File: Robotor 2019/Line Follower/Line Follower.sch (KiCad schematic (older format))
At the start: 70 parts, among them J1 Conn_01x03_Male, J2 Conn_01x04_Female, J3 USB_B_Mini, J7 Conn_01x03_Female, J8 Conn_01x03_Female, M1 Motor_DC, M2 Motor_DC, U1 AMS1117-3V3, U2 AMS1117-3V3, U3 AMS1117-5.0, U4 STM32F103C8Tx, U5 ITR8307, U6 L298P, U7 ITR8307, U8 ITR8307, U9 ITR8307, Y1 32.768Khz, Y2 8Mhz

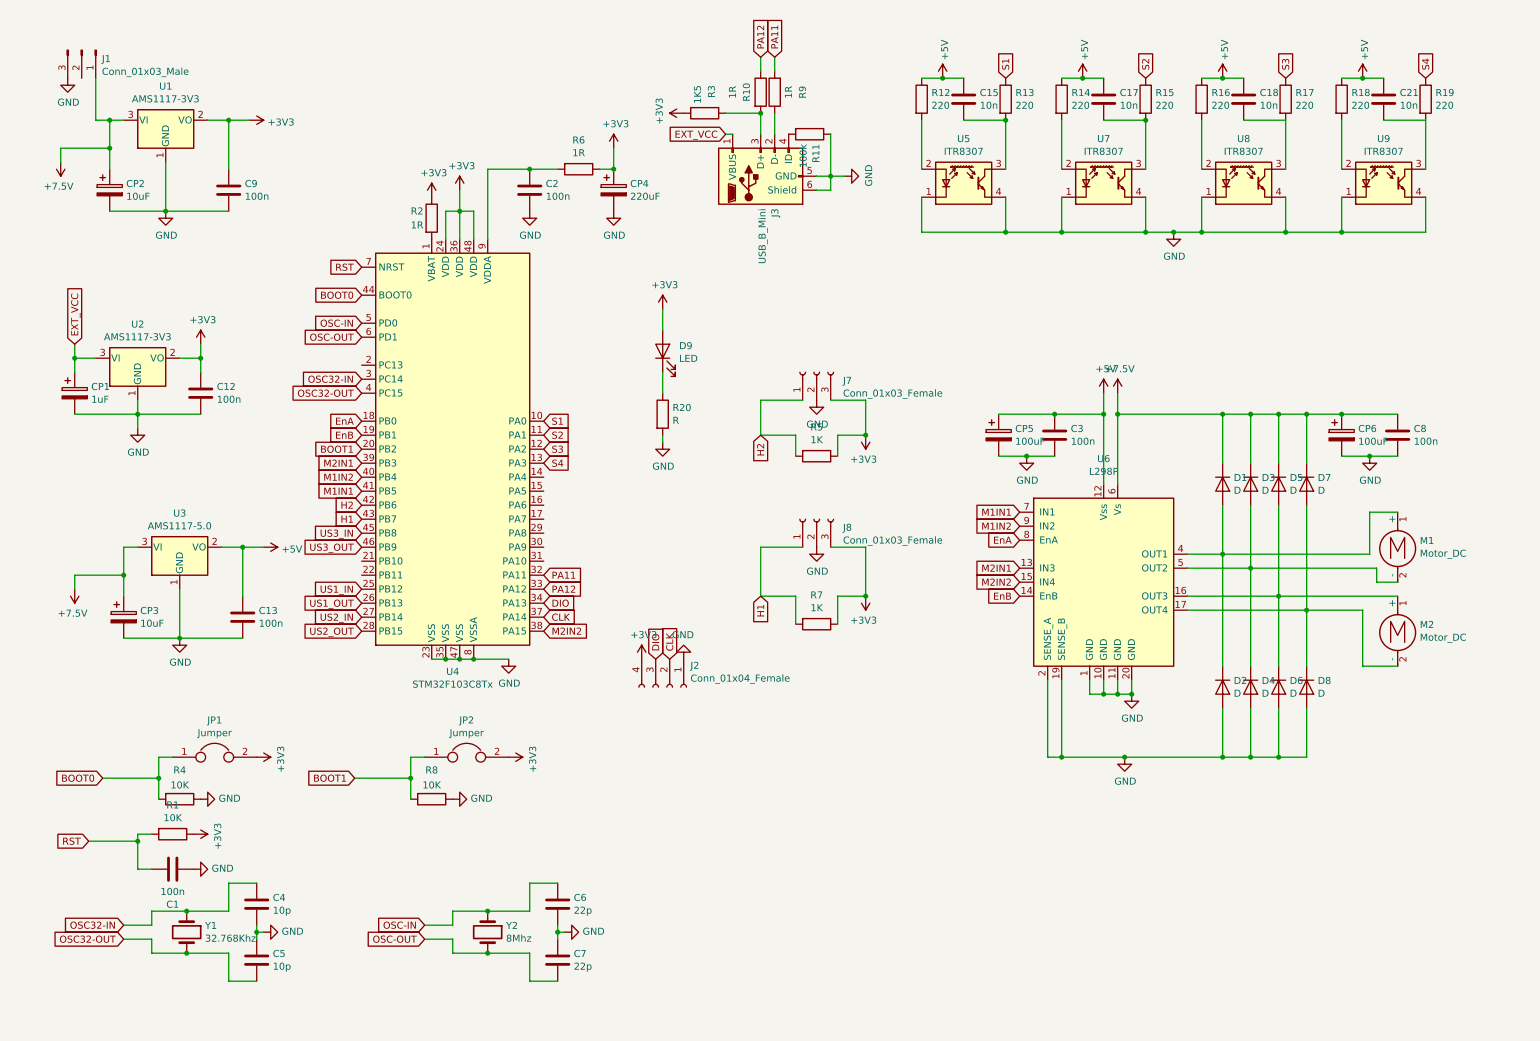
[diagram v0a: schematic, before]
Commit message: Hopefully it works, Line Follower scheme added.
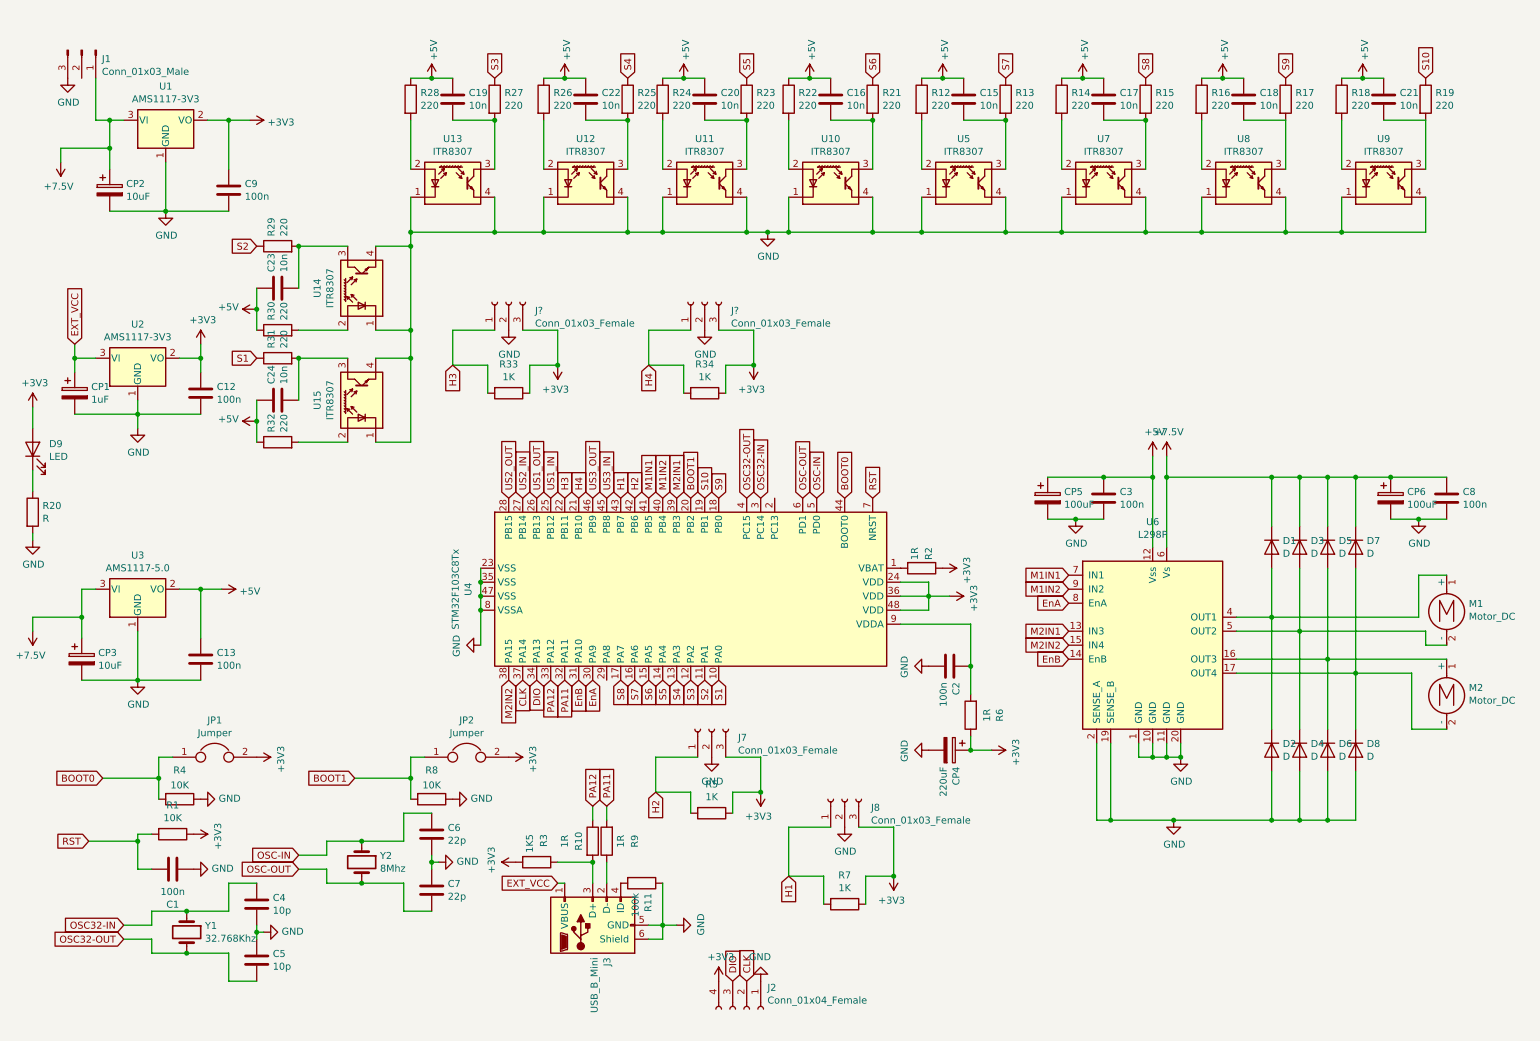
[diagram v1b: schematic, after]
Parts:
- added C16, C19, C20, C22, C23, C24: 10n, Capacitor_SMD:C_0805_2012Metric_Pad1.15x1.40mm_HandSolder, symbol Device:C
- added J? (x2): Conn_01x03_Female, Connector_PinHeader_2.54mm:PinHeader_1x03_P2.54mm_Vertical, symbol Connector:Conn_01x03_Female
- added R21, R22, R23, R24, R25, R26, R27, R28, R29, R30, R31, R32: 220, Resistor_SMD:R_0805_2012Metric_Pad1.15x1.40mm_HandSolder, symbol Device:R
- added R33, R34: 1K, Resistor_SMD:R_0805_2012Metric_Pad1.15x1.40mm_HandSolder, symbol Device:R
- added U10, U11, U12, U13, U14, U15: ITR8307, OptoDevice:Everlight_ITR8307, symbol Sensor_Proximity:ITR8307
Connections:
- net +3V3: now also J?.3 (Pin_3), J?.3 (Pin_3), R33.1, R34.1
- net +5V: now also C16.1, C19.1, C20.1, C22.1, C23.1, C24.1, R22.1, R24.1, R26.1, R28.1, R30.1, R32.1
- net EnA: now also U4.30 (PA9); no longer U4.18 (PB0)
- net EnB: now also U4.31 (PA10); no longer U4.19 (PB1)
- net GND: now also J?.2 (Pin_2), J?.2 (Pin_2), U10.1 (K), U10.4 (E), U11.1 (K), U11.4 (E), U12.1 (K), U12.4 (E), U13.1 (K), U13.4 (E), U14.1 (K), U14.4 (E), U15.1 (K), U15.4 (E)
- net S1: now also R31.1; no longer R13.1
- net S2: now also R29.1; no longer R15.1
- net S3: now also R27.1; no longer R17.1
- net S4: now also R25.1; no longer R19.1
- net S5: now reaches U4.14 (PA4)
- net S5: now also R23.1
- net S6: now reaches U4.15 (PA5)
- net S6: now also R21.1
- net S7: now reaches U4.16 (PA6)
- net S7: now also R13.1
- net S8: now reaches U4.17 (PA7)
- net S8: now also R15.1
- net H4: now reaches U4.21 (PB10)
- net H4: now also J?.1 (Pin_1), R34.2
- net H3: now reaches U4.22 (PB11)
- net H3: now also J?.1 (Pin_1), R33.2
- new net: R22.2, U10.2 (A)
- new net: C16.2, R21.2, U10.3 (C)
- new net: R24.2, U11.2 (A)
- new net: C20.2, R23.2, U11.3 (C)
- new net: R26.2, U12.2 (A)
- new net: C22.2, R25.2, U12.3 (C)
- new net: R28.2, U13.2 (A)
- new net: C19.2, R27.2, U13.3 (C)
- new net: R30.2, U14.2 (A)
- new net: C23.2, R29.2, U14.3 (C)
- new net: R32.2, U15.2 (A)
- new net: C24.2, R31.2, U15.3 (C)
- new net S10: R19.1, U4.19 (PB1)
- new net S9: R17.1, U4.18 (PB0)
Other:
- moved on the sheet: C13, C2, C3, C6, C7, C8, CP3, CP4, CP5, CP6, D1, D2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

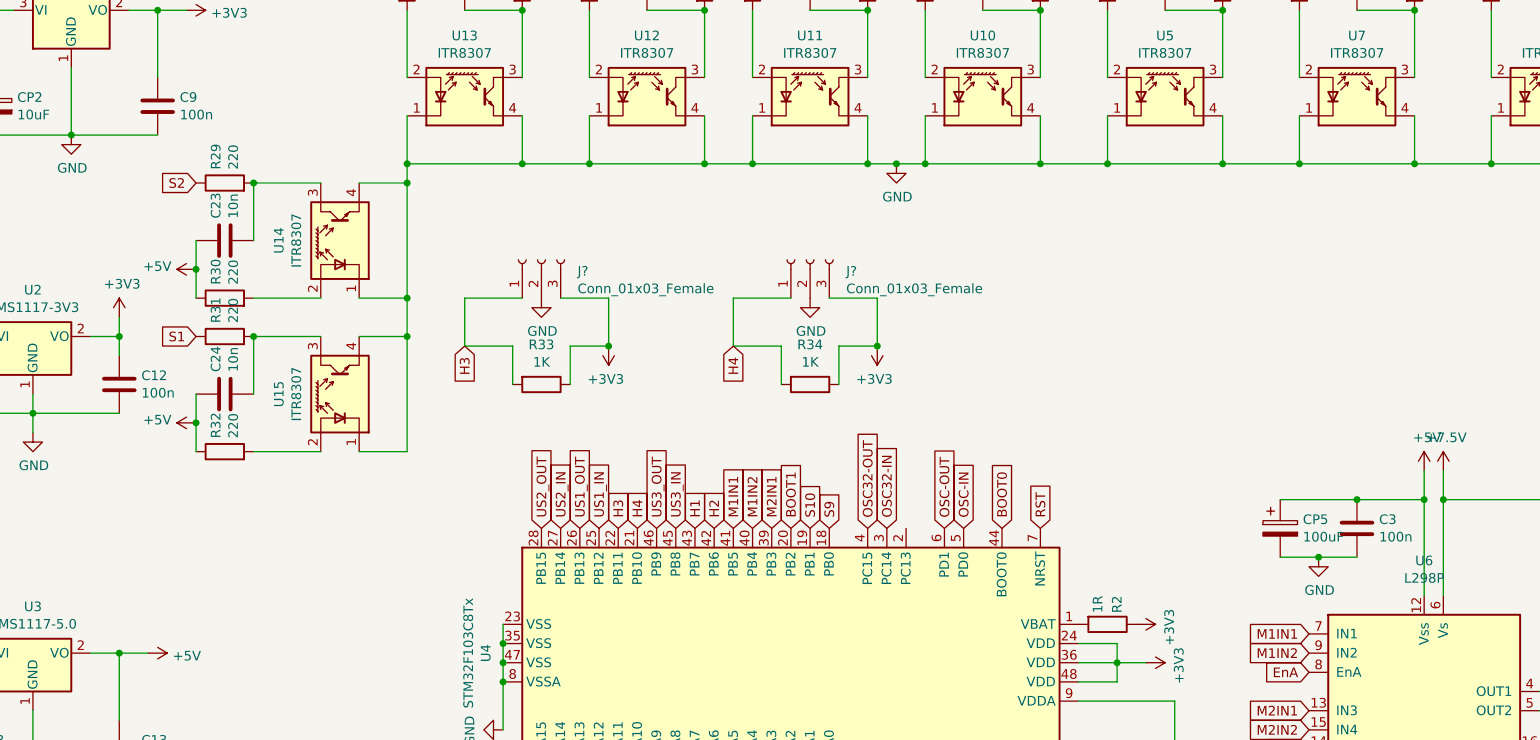
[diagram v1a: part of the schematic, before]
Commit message: Updated electric schematic for tribot with 2 floors.
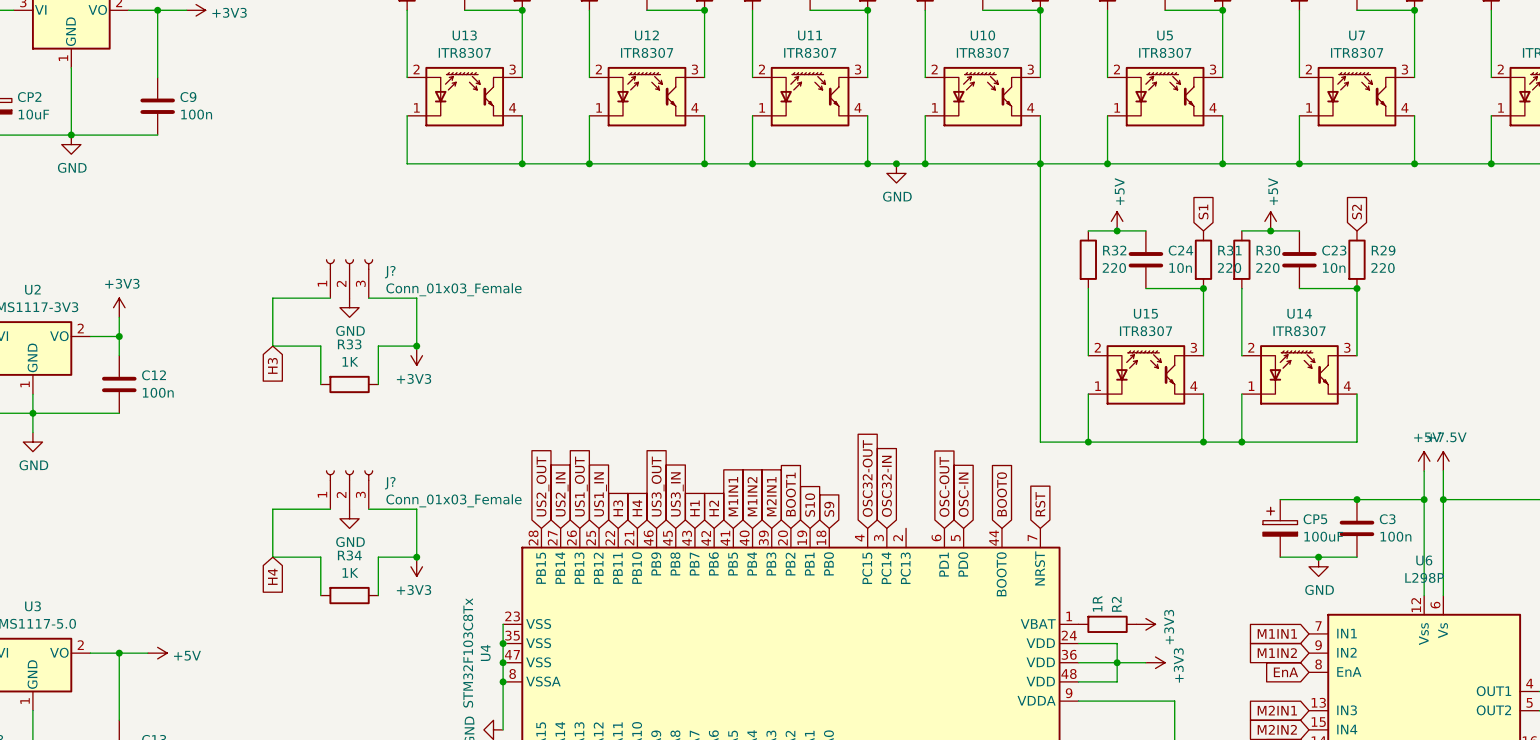
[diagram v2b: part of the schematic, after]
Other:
- moved on the sheet: C23, C24, J?, R29, R30, R31, R32, R33, R34, U14, U15

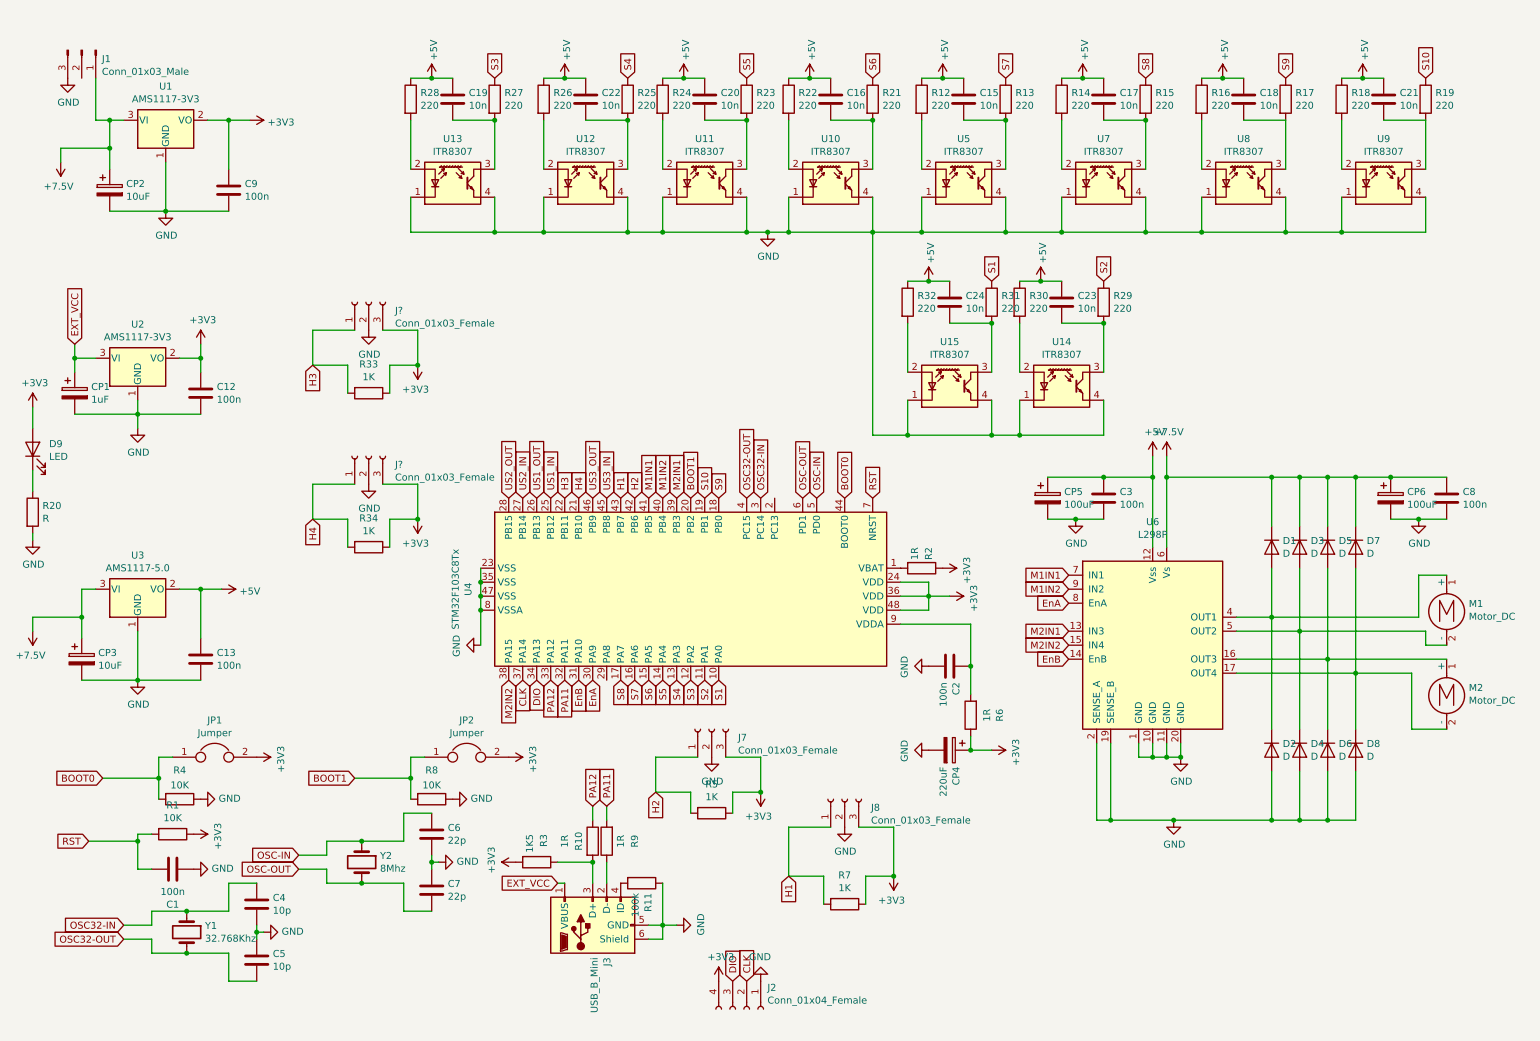
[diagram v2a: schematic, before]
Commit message: Tidied up line follower eschema: - Moved components around. - Removed USB voltage regulator. - Added USB power output to battery voltage regulator.
Annotated components in eschema, assigned footprints, created a netlist.
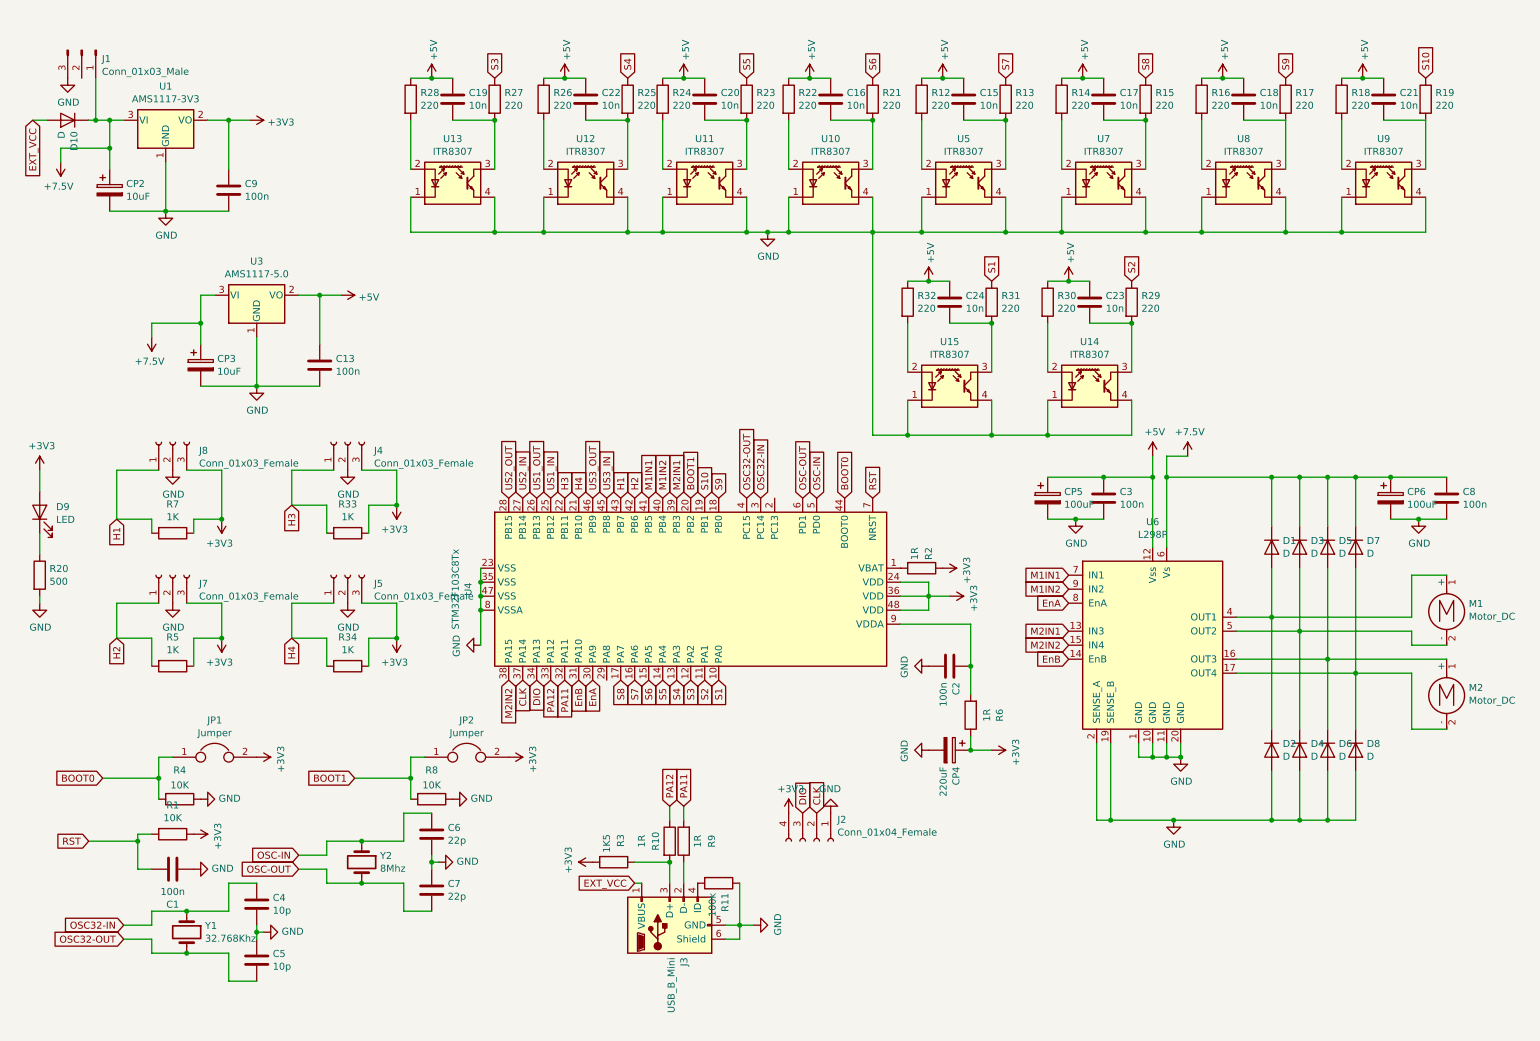
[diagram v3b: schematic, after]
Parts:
- removed C12: 100n, Capacitor_SMD:C_0805_2012Metric_Pad1.15x1.40mm_HandSolder, symbol Device:C
- removed CP1: 1uF, Capacitor_SMD:CP_Elec_4x5.3, symbol Device:CP
- removed U2: AMS1117-3V3, Package_TO_SOT_SMD:SOT-223-3_TabPin2, symbol Regulator_Linear:AMS1117-5.0
- added D10: D, Diode_THT:D_A-405_P5.08mm_Vertical_AnodeUp, symbol Device:D
- D1, D2, D3, D4, D5, D6, D7, D8: footprint Diode_THT:D_DO-15_P5.08mm_Vertical_AnodeUp -> Diode_THT:D_A-405_P5.08mm_Vertical_AnodeUp
- R20: value R -> 500
- gave numbers to parts that had none: 2
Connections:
- net +7.5V: now also D10.1 (K)
- net EXT_VCC: now also D10.2 (A)
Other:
- moved on the sheet: C13, C23, CP3, D9, J2, J3, J4, J5, J7, J8, R10, R11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
